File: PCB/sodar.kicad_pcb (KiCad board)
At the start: 2 copper layers, 71 parts, among them J1 Screw_Terminal_01x02, J2 Conn_02x12_Counter_Clockwise, J3 Conn_01x02, U1 TC78H621FNG, U10 TC78H621FNG, U2 TC78H621FNG, U3 TC78H621FNG, U4 TC78H621FNG, U5 TC78H621FNG, U6 TC78H621FNG, U7 TC78H621FNG, U8 TC78H621FNG, U9 TC78H621FNG

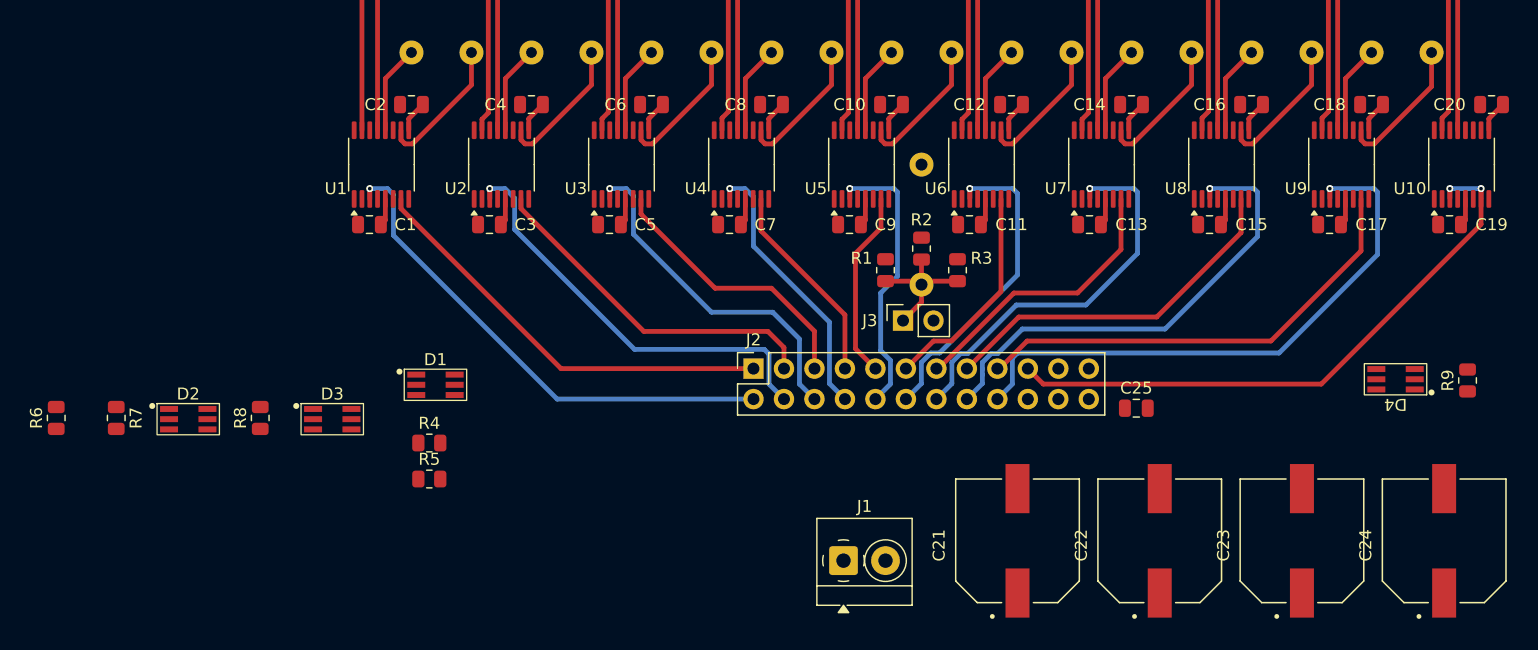
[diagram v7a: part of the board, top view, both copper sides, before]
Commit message: Movec components & connected STBY signal
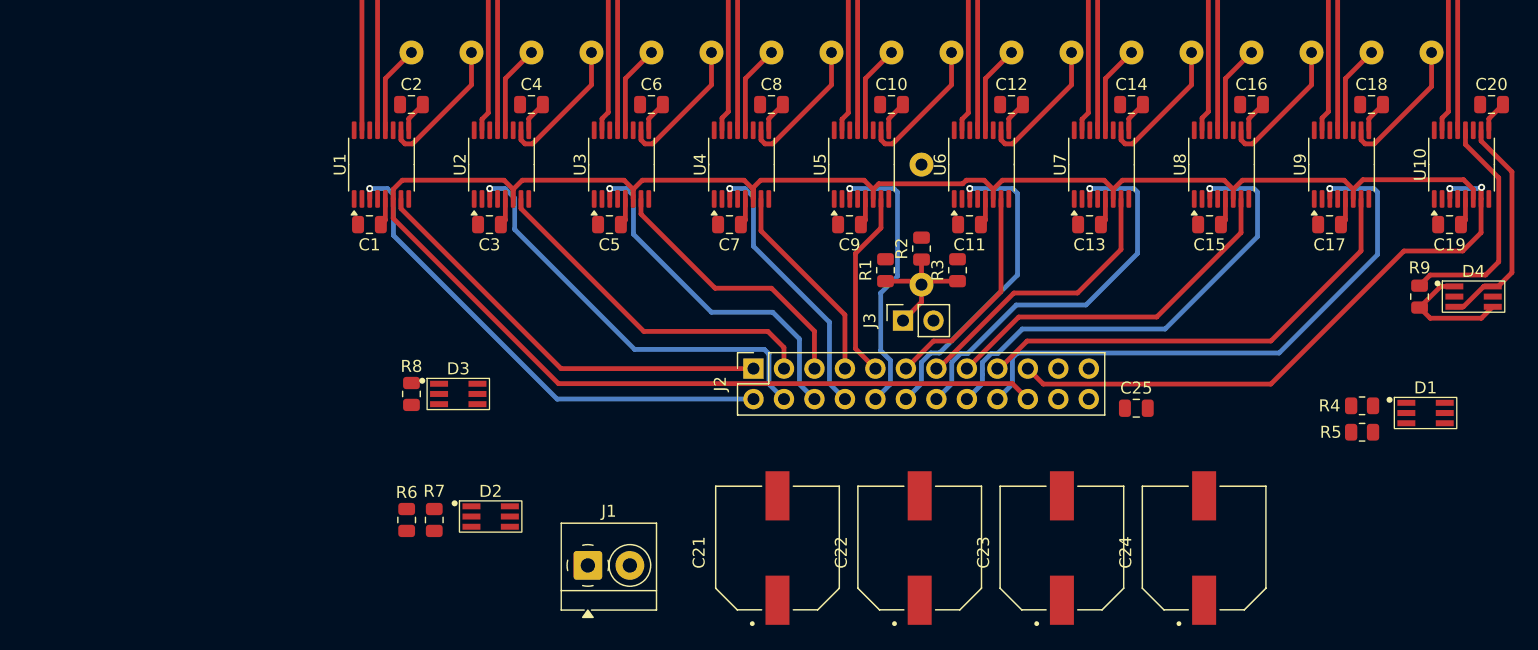
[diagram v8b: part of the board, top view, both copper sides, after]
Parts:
- moved D1 82.6 mm to (192.0, 73.7)
- moved R5 77.8 mm to (186.7, 75.3)
- moved R4 77.8 mm to (186.7, 73.1)
- moved R6 30.4 mm to (107.1, 82.6)
- moved R7 27.8 mm to (109.4, 82.6)
- moved D2 27.2 mm to (114.1, 82.3)
- moved J1 21.3 mm to (122.2, 86.4)
- moved C21 20.0 mm to (138.0, 85.0)
- moved C22 20.0 mm to (149.8, 85.0)
- moved C23 20.0 mm to (161.7, 85.0)
- moved C24 20.0 mm to (173.6, 85.0)
- moved R8 12.8 mm to (107.5, 72.1)
- moved D4 11.1 mm to (196.0, 64.0), turned to 0 degrees
- moved D3 10.5 mm to (111.4, 72.1)
- moved R9 8.05 mm to (191.5, 64.0), turned to -90 degrees
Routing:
- net STBY: track 0.00 -> 165.3 mm
- net PHA_LED1: track 0.00 -> 19.5 mm
- net PHA_LED2: track 0.00 -> 18.9 mm
- net Net-(D4-B-): track 0.00 -> 10.5 mm
- net S19: track 50.3 -> 50.9 mm
